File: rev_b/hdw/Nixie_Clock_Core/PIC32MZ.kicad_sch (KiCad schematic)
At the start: 3 parts, among them U1001 PIC32MZ2048EFG100_IPF

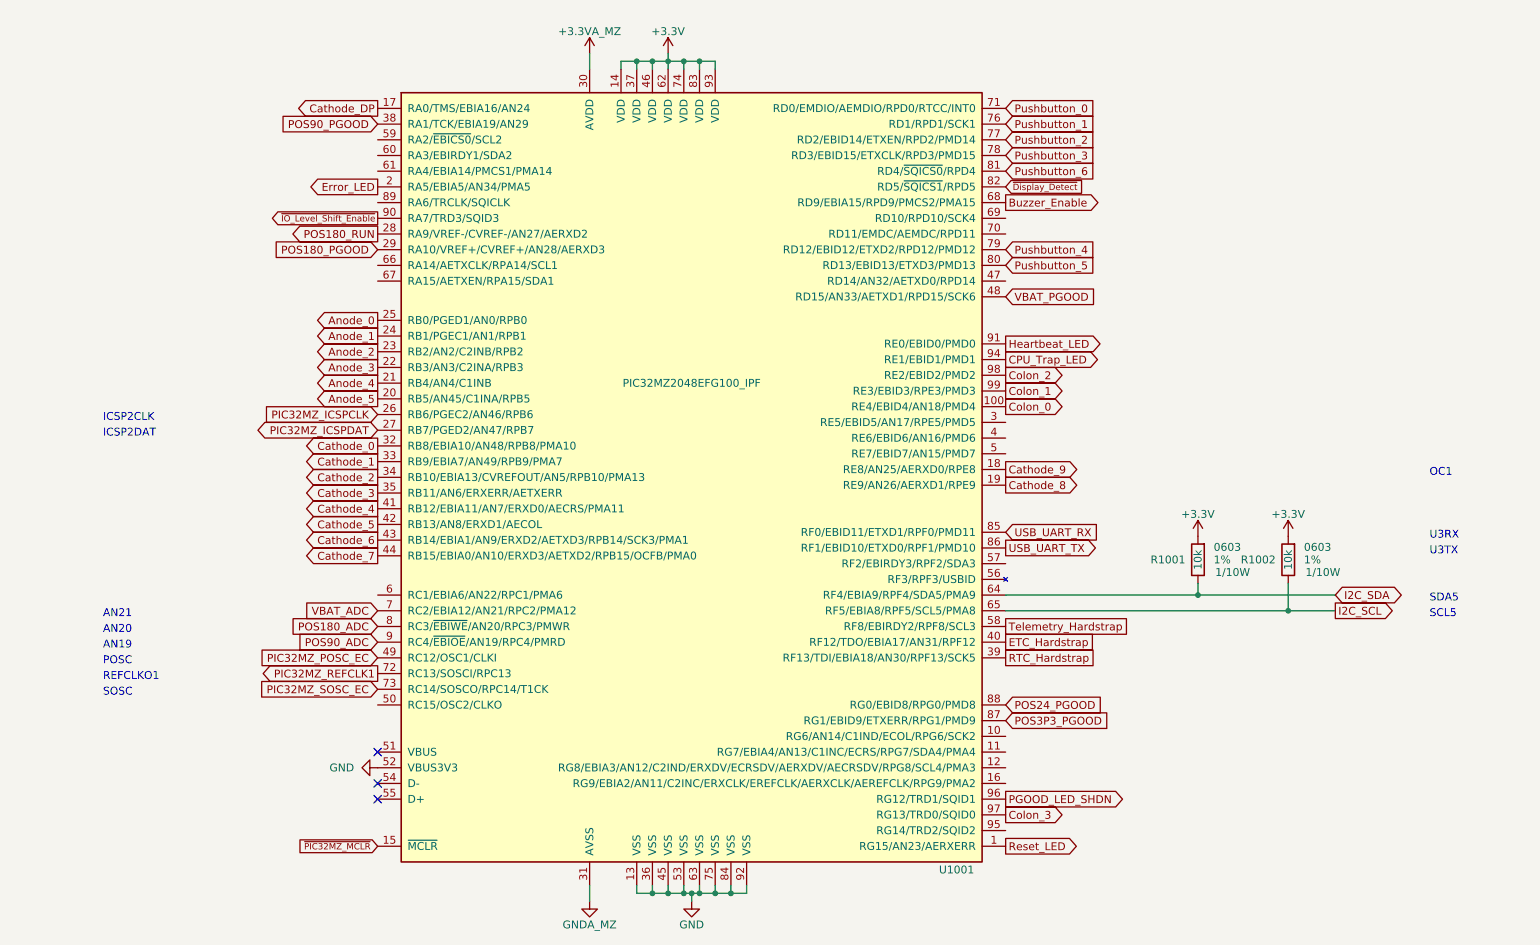
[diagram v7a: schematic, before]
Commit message: added BOM
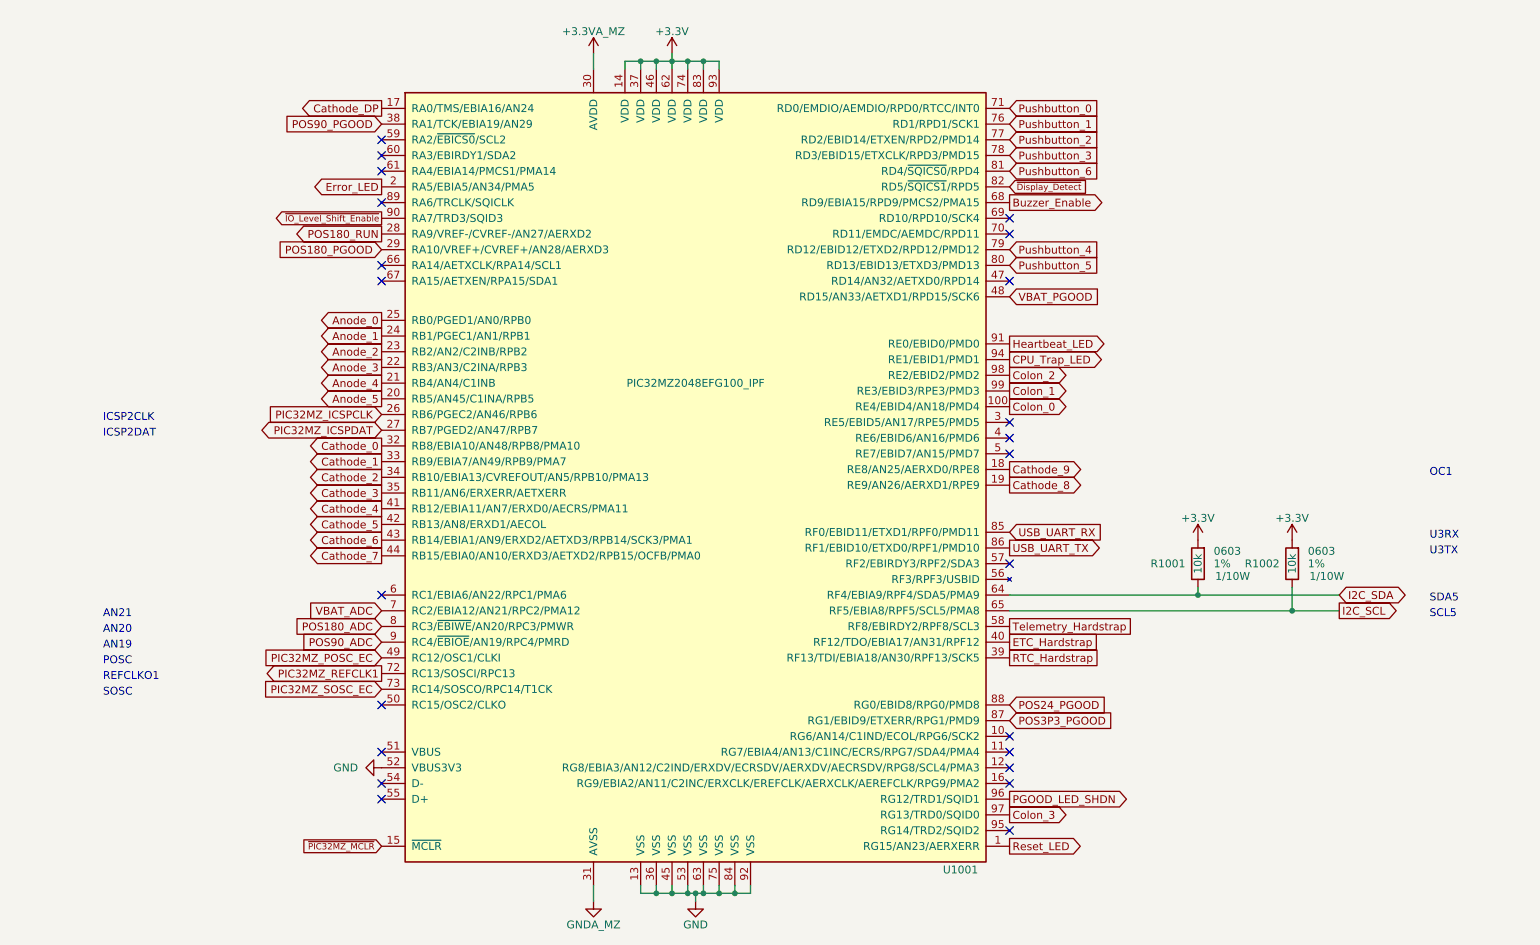
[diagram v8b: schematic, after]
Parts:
- R1001, R1002: Digi-Key PN (none) -> 541-10.0KHCT-ND
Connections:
- no-connect marks 3 -> 23
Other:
- title: (none) -> Nixie Clock Redux Core Board
- moved on the sheet: R1001, R1002, U1001
